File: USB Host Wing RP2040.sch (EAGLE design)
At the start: 59 parts, among them IC1 RP2040_QFN56, J1 USB_A_SMT_FEMALE, Q3 DMG341, SW1 KMR2, SW2 KMR2, U1 2MB Flash, U2 AP2112-3.3, U3 PCA9410AUKZ, X6 USB Type C, Y1 12MHZ

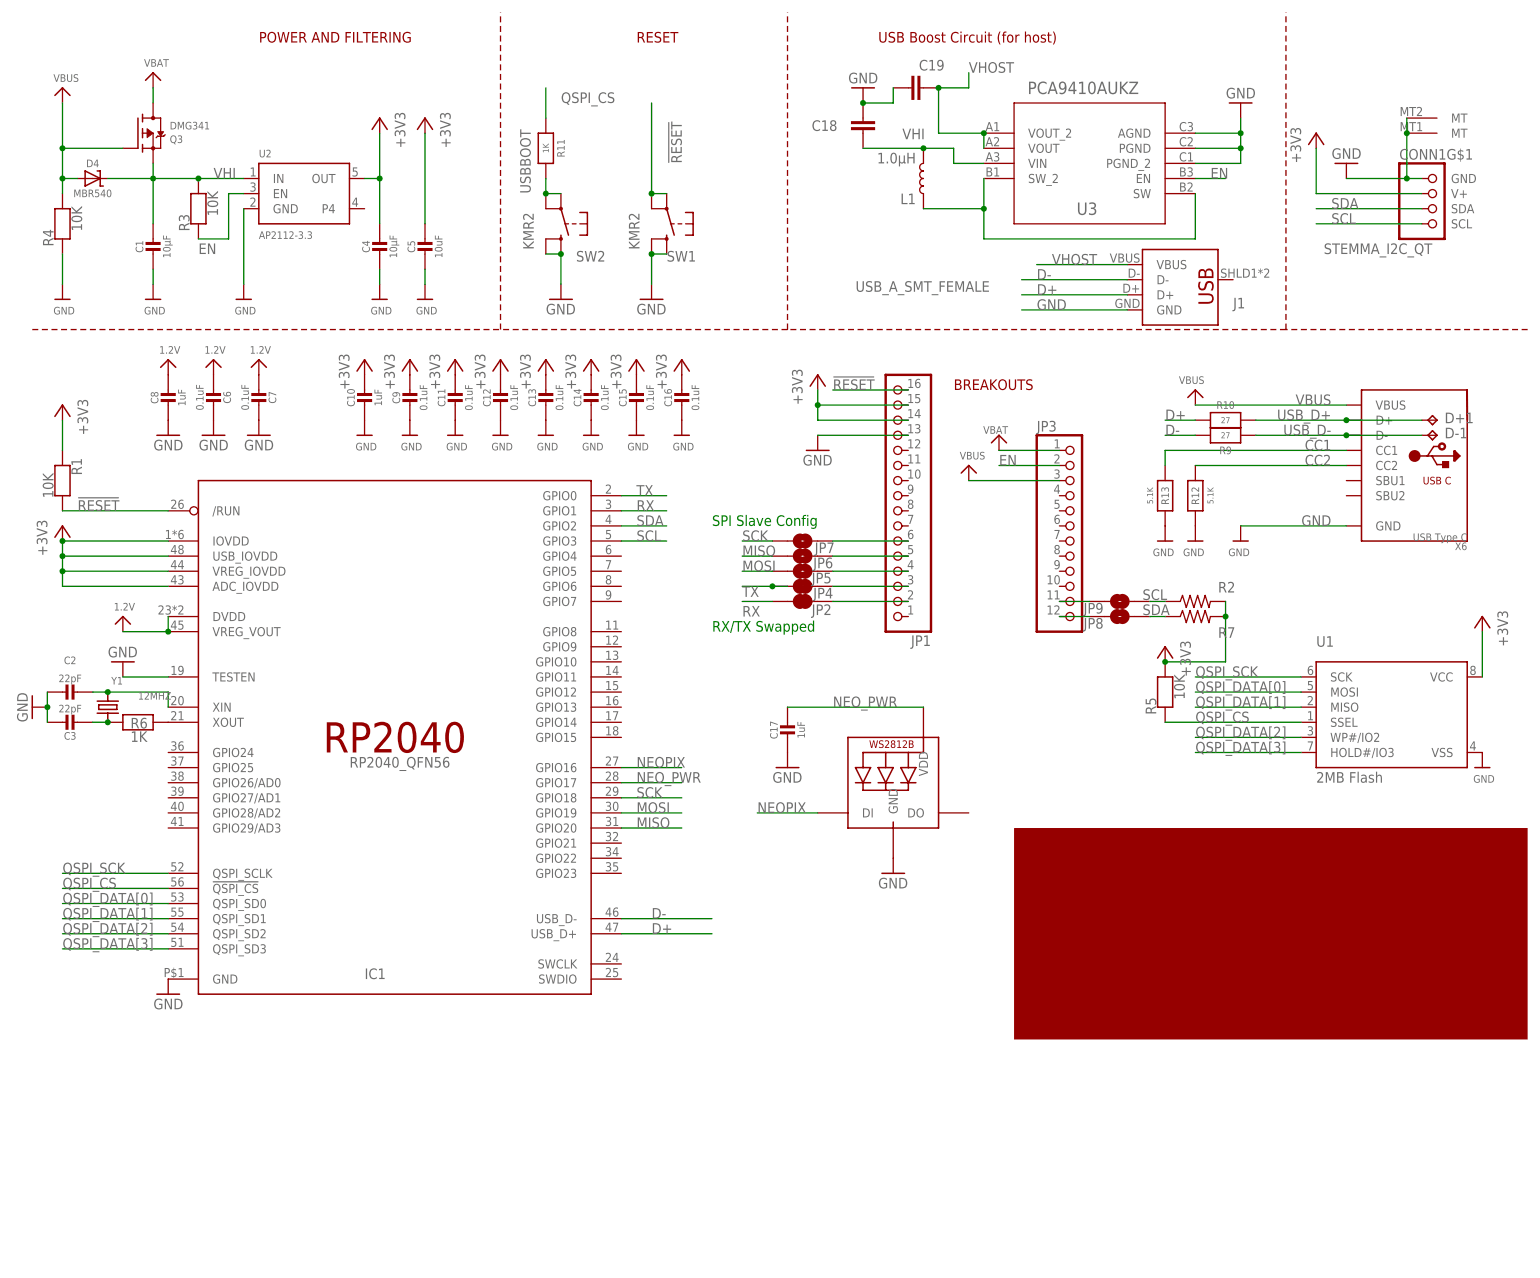
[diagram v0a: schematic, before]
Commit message: Continued fixes
Modified to replace the boost converter and fix the MOSI/MISO issue.  Also added CS jumpers for SPI users.
Still has air wires & issues.
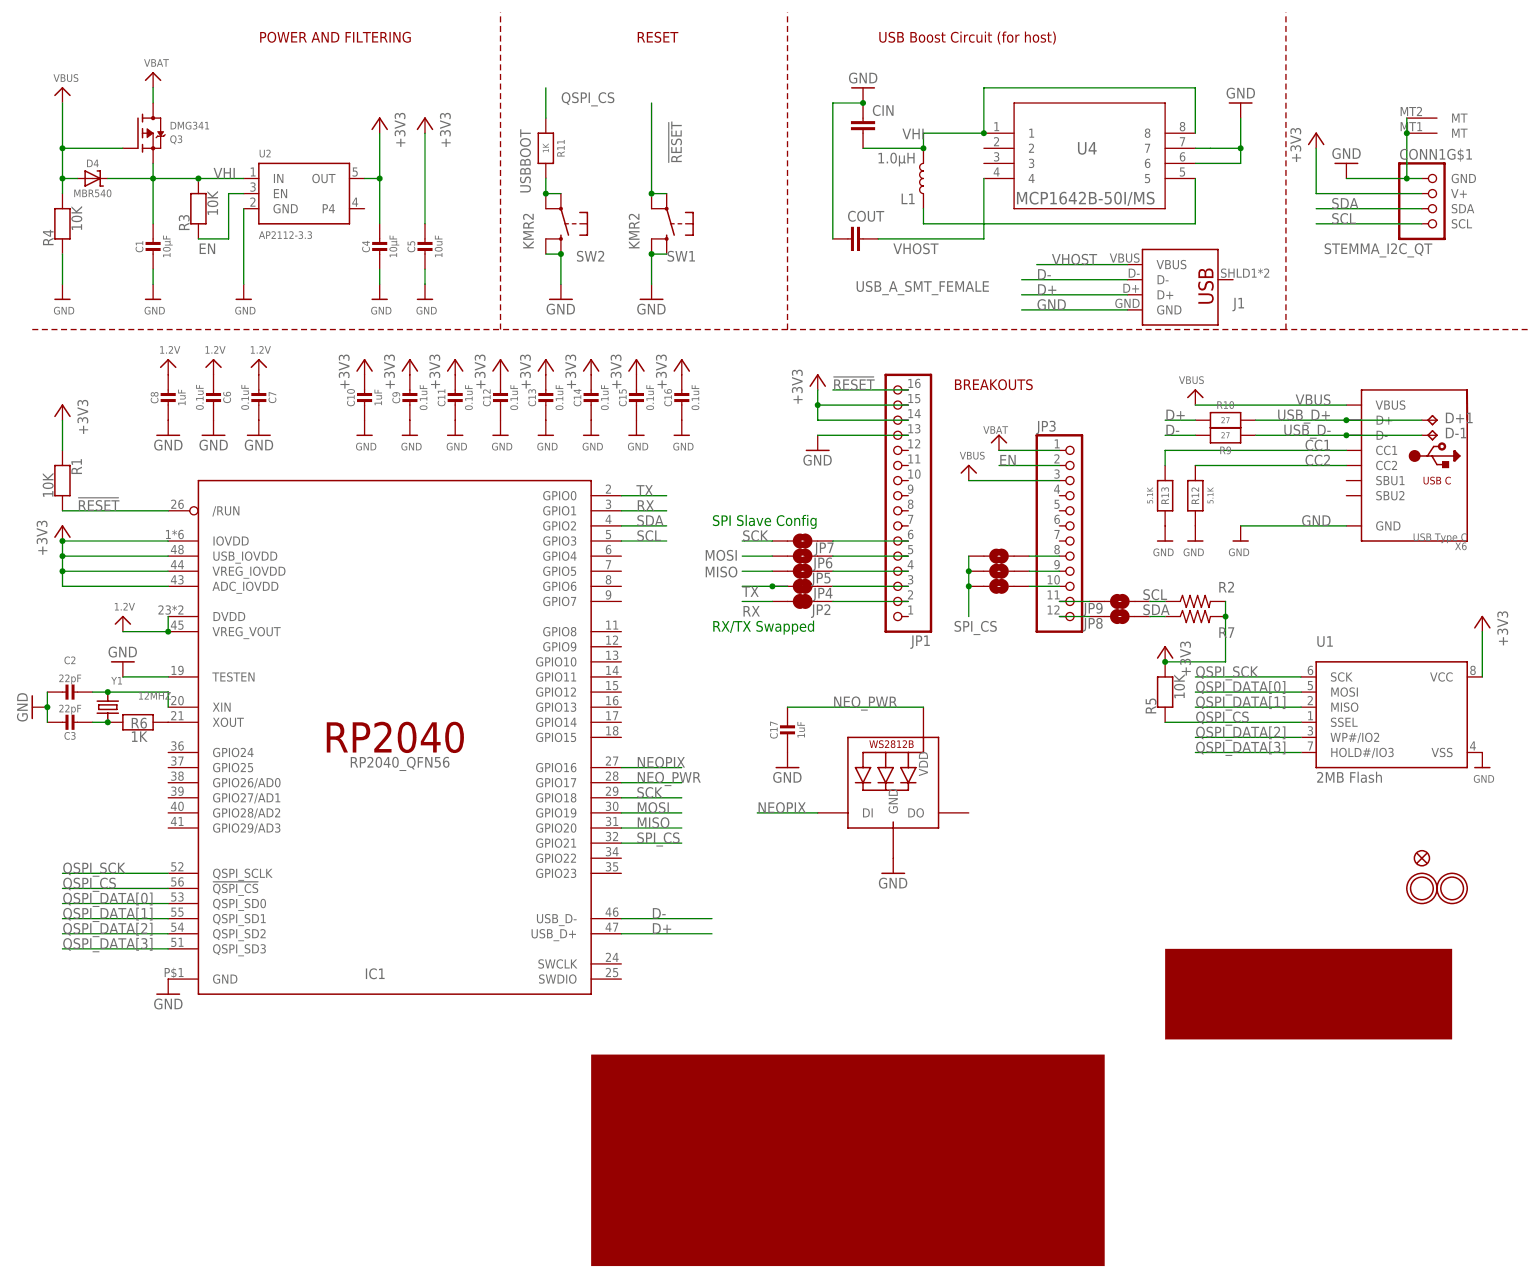
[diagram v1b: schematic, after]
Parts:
- removed C19: (no value), DECADE:SPARKFUN_CAP0603-CAP
- removed U3: PCA9410AUKZ, PCA9411:PCA9410AUKZ
- added COUT: (no value), DECADE:SPARKFUN_CAP0603-CAP
- added JP10, JP11, JP12: JUMPER-SMT_2_NO_SILK, SparkFun-Jumpers:JUMPER-SMT_2_NO_SILK
- added U4: MCP1642B-50I/MS, ATMakers:MCP1642B-50I/MS
- renumbered C18 to CIN
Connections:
- new net N$12: JP12.2, JP3.8
- new net N$13: JP11.2, JP3.9
- new net N$14: JP10.2, JP3.10
- new net SPI_CS: IC1.GPIO21, JP10.1, JP11.1, JP12.1
- net EN: no longer U3.EN
- net GND: now also COUT.1, U4.6, U4.7; no longer C19.1, U3.AGND, U3.PGND, U3.PGND_2
- net MISO: now also JP5.1; no longer JP6.1
- net MOSI: now also JP6.1; no longer JP5.1
- net N$10: now also U4.5; no longer U3.SW, U3.SW_2
- net VHI: now also U4.1, U4.8; no longer U3.VIN
- net VHOST: now also COUT.2, U4.4; no longer C19.2, U3.VOUT, U3.VOUT_2

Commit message: Update for John
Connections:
- net VBUS: no longer X6.VBUS
- net VHOST: now also X6.VBUS
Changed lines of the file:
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@@
 <part name="U$24" library="microbuilder" deviceset="GND" device=""/>
 <part name="U$41" library="microbuilder" deviceset="GND" device=""/>
-<part name="U$44" library="microbuilder" deviceset="VBUS" device=""/>
 <part name="IC1" library="adafruit_micro" deviceset="RP2040" device="_QFN56"/>
 <part name="R1" library="microbuilder" deviceset="RESISTOR" device="_0603_NOOUT" value="10K"/>
@@
 <attribute name="VALUE" x="209.804" y="83.82" size="1.27" layer="96" rot="MR0"/>
 </instance>
-<instance part="U$44" gate="G$1" x="200.66" y="111.76" smashed="yes" rot="MR0">
-<attribute name="VALUE" x="202.184" y="112.776" size="1.27" layer="96" rot="MR0"/>
-</instance>
 <instance part="IC1" gate="G$1" x="66.04" y="53.34" smashed="yes">
 <attribute name="NAME" x="60.96" y="12.7" size="1.778" layer="95"/>
@@
 <pinref part="R4" gate="G$1" pin="2"/>
 </segment>
-<segment>
-<wire x1="200.66" y1="109.22" x2="226.06" y2="109.22" width="0.1524" layer="91"/>
-<pinref part="X6" gate="G$1" pin="VBUS"/>
-<label x="223.52" y="109.22" size="1.778" layer="95" rot="MR0"/>
-<pinref part="U$44" gate="G$1" pin="VBUS"/>
-</segment>
 </net>
 <net name="VBAT" class="1">
@@
 <label x="176.53" y="132.842" size="1.778" layer="95"/>
 </segment>
-</net>
+<segment>
+<pinref part="X6" gate="G$1" pin="VBUS"/>
+<wire x1="226.06" y1="109.22" x2="213.36" y2="109.22" width="0.1524" layer="91"/>
+<label x="213.36" y="109.22" size="1.778" layer="95"/>
+</segment>
+</net>

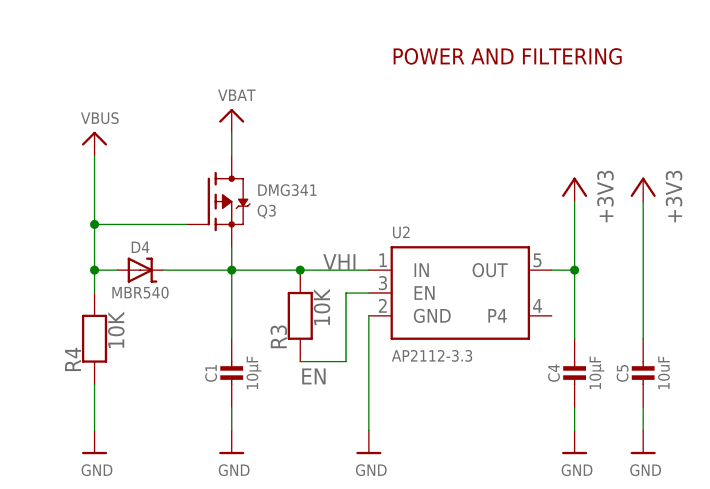
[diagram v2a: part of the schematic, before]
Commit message: Changed source of linear regulator to VHOST
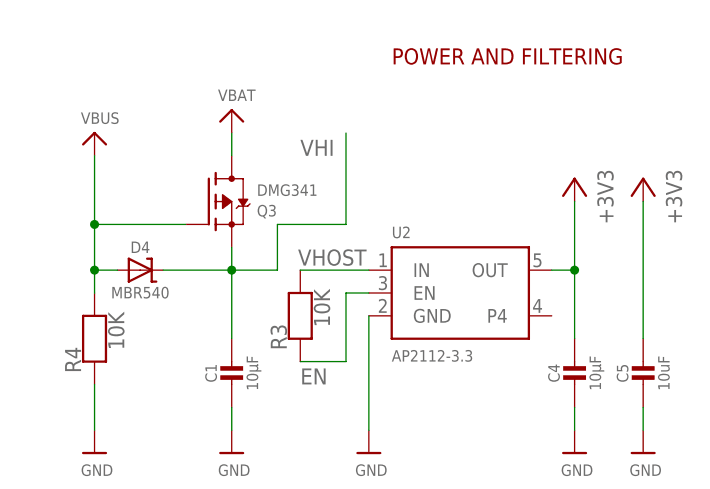
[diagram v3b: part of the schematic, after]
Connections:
- net VHI: no longer R3.2, U2.IN
- net VHOST: now also R3.2, U2.IN
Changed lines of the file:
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@@
 <setting verticaltext="up"/>
 </settings>
-<grid distance="0.1" unitdist="inch" unit="mil" style="lines" multiple="1" display="no" altdistance="0.01" altunitdist="inch" altunit="inch"/>
+<grid distance="0.1" unitdist="inch" unit="inch" style="lines" multiple="1" display="no" altdistance="0.01" altunitdist="inch" altunit="inch"/>
 <layers>
 <layer number="1" name="Top" color="4" fill="1" visible="no" active="no"/>
@@
 <wire x1="25.4" y1="149.86" x2="25.4" y2="147.32" width="0.1524" layer="91"/>
 <pinref part="C1" gate="G$1" pin="1"/>
-<wire x1="40.64" y1="147.32" x2="33.02" y2="147.32" width="0.1524" layer="91"/>
-<wire x1="33.02" y1="147.32" x2="25.4" y2="147.32" width="0.1524" layer="91"/>
 <wire x1="25.4" y1="147.32" x2="25.4" y2="139.7" width="0.1524" layer="91"/>
-<pinref part="U2" gate="G$1" pin="IN"/>
 <junction x="25.4" y="147.32"/>
-<pinref part="R3" gate="G$1" pin="2"/>
-<junction x="33.02" y="147.32"/>
-<label x="35.56" y="147.32" size="1.778" layer="95"/>
+<wire x1="25.4" y1="147.32" x2="30.48" y2="147.32" width="0.1524" layer="91"/>
+<wire x1="30.48" y1="147.32" x2="30.48" y2="152.4" width="0.1524" layer="91"/>
+<wire x1="30.48" y1="152.4" x2="38.1" y2="152.4" width="0.1524" layer="91"/>
+<wire x1="38.1" y1="152.4" x2="38.1" y2="162.56" width="0.1524" layer="91"/>
+<label x="33.02" y="160.02" size="1.778" layer="95"/>
 </segment>
 <segment>
@@
 <label x="213.36" y="109.22" size="1.778" layer="95"/>
 </segment>
-</net>
+<segment>
+<pinref part="U2" gate="G$1" pin="IN"/>
+<wire x1="40.64" y1="147.32" x2="33.02" y2="147.32" width="0.1524" layer="91"/>
+<pinref part="R3" gate="G$1" pin="2"/>
+<label x="32.766" y="147.828" size="1.778" layer="95"/>
+</segment>
+</net>
